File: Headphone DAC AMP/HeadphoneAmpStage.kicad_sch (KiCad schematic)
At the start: 66 parts, among them U3 TPA6120A2DWP, U4 OPA1612AxD, U5 OPA1612AxD

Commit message: Cleaned up shcematic more
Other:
- note added: "Amplifier Decoupling"
- note added: "Analog Filtering"
- note added: "Filter Decoupling"
- note added: "Headphone Amplifier"
- moved on the sheet: C25, C26, C27, C28, C29, C30, C31, C32, C5, C6, C7, C8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

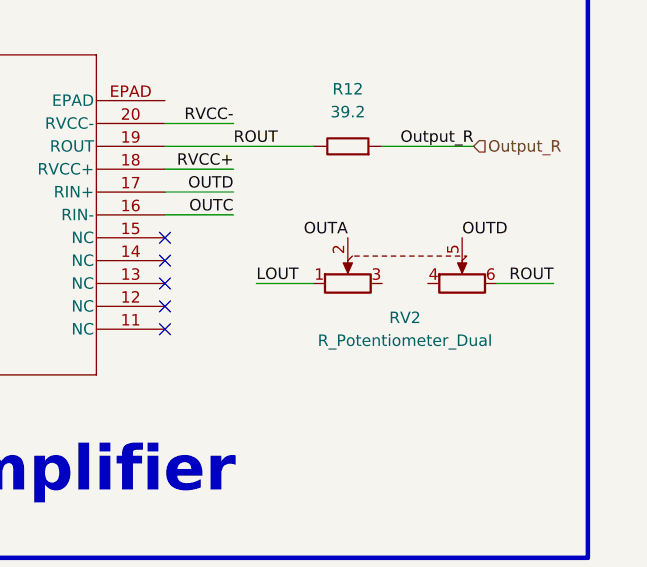
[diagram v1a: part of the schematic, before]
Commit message: Cleaned Up and Annotated Schematic
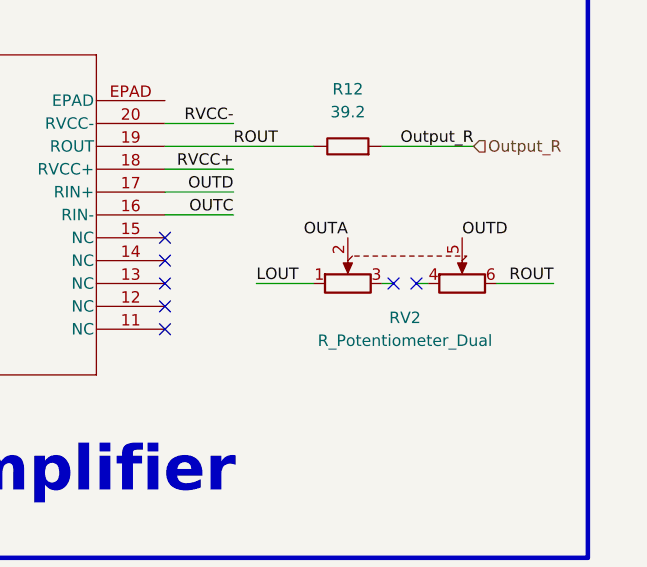
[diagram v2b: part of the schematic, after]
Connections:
- no-connect marks 10 -> 12
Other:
- company: (none) -> Personal Project - Kettering University
- title: (none) -> Hi-Fidelity USB DAC Amplifier
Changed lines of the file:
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@@
 	(generator_version "9.0")
 	(paper "A4")
+	(title_block
+		(title "Hi-Fidelity USB DAC Amplifier")
+		(date "2025-11-19")
+		(rev "1.0")
+		(company "Personal Project - Kettering University")
+		(comment 1 "Designed by Dan Abidov & Luke Stirzinger")
+		(comment 2 "Based on XMOS Xu316 and ES9039Q2M")
+	)
 	(rectangle
 		(start 12.7 12.7)
@@
 	)
 	(no_connect
+		(at 264.16 46.99)
+	)
+	(no_connect
 		(at 170.18 46.99)
 	)
@@
 	)
 	(no_connect
+		(at 261.62 46.99)
+	)
+	(no_connect
 		(at 236.22 41.91)
 	)
@@
 	(wire
 		(pts
+			(xy 264.16 46.99) (xy 265.43 46.99)
+		)
+		(stroke
+			(width 0)
+			(type default)
+		)
+	)
+	(wire
+		(pts
 			(xy 40.64 106.68) (xy 41.91 106.68)
 		)
@@
 	(wire
 		(pts
+			(xy 261.62 46.99) (xy 260.35 46.99)
+		)
+		(stroke
+			(width 0)
+			(type default)
+		)
+	)
+	(wire
+		(pts
 			(xy 243.84 36.83) (xy 236.22 36.83)
 		)
@@
 			"AAAAAAAAAAAAAAAAAAAAAAAAAAAAAAAAAAAAAAAAAAAAAAAAAAAAAAAAAAAAAAAAAAAAAAAAAAAA"
 			"AAAAAAAAAAAAAAAAAAAAAAAAAAAAAAAAAAAAAAAAAAAAAAAAAAAAAAAAAAAAAAAAAAAAAAAAAAAA"
+			"AAAAAAAAAAAAAAAAAAAAAAAAAAAAAAAAAAAAAAAAAAAAAAAAAAAAAAAAAAAAAAAAAAAAAAAAAAAA"
+			"AAAAAAAAAAAAAAAAAAAAAAAAAAAAAAAAAAAAAAAAAAAAAAAAAAAAAAAAAAAAAAAAAAAAAAAAAAAA"
+			"AAAAAAAAAAAAAAAAAAAAAAAAAAAAAAAAAAAAAAAAAAAAAAAAAAAAAAAAAAAAAAAAAAAAAAAAAAAA"
+			"AAAAAAAAAAAAAAAAAAAAAAAAAAAAAAAAAAAAAAAAAAAAAAAAAAAAAAAAAAAAAAAAAAAAAAAAAAAA"
+			"AAAAAAAAAAAAAAAAAAAAAAAAAAAAAAAAAAAAAAAAAAAAAAAAAAAAAAAAAAAAAAAAAAAAAAAAAAAA"
+			"AAAAAAAAAAAAAAAAAAAAAAAAAAAAAAAAAAAAAAAAAAAAAAAAAAAAAAAAAAAAAAAAAAAAAAAAAAAA"
+			"AAAAAAAAAAAAAAAAAAAAAAAAAAAAAAAAAAAAAAAAAAAAAAAAAAAAAAAAAAAAAAAAAAAAAAAAAAAA"
+			"AAAAAAAAAAAAAAAAAAAAAAAAAAAAAAAAAAAAAAAAAAAAAAAAAAAAAAAAAAAAAAAAAAAAAAAAAAAA"
+			"AAAAAAAAAAAAAAAAAAAAAAAAAAAAAAAAAAAAAAAAAAAAAAAAAAAAAAAAAAAAAAAAAAAAAAAAAAAA"
+			"AAAAAAAAAAAAAAAAAAAAAAAAAAAAAAAAAAAAAAAAAAAAAAAAAAAAAAAAAAAAAAAAAAAAAAAAAAAA"
+			"AAAAAAAAAAAAAAAAAAAAAAAAAAAAAAAAAAAAAAAAAAAAAAAAAAAAAAAAAAAAAAAAAAAAAAAAAAAA"
+			"AAAAAAAAAAAAAAAAAAAAAAAAAAAAAAAAAAAAAAAAAAAAAAAAAAAAAAAAAAAAAAAAAAAAAAAAAAAA"
+			"AAAAAAAAAAAAAAAAAAAAAAAAAAAAAAAAAAAAAAAAAAAAAAAAAAAAAAAAAAAAAAAAAAAAAAAAAAAA"
+			"AAAAAAAAAAAAAAAAAAAAAAAAAAAAAAAAAAAAAAAAAAAAAAAAAAAAAAAAAAAAAAAAAAAAAAAAAAAA"
+			"AAAAAAAAAAAAAAAAAAAAAAAAAAAAAAAAAAAAAAAAAAAAAAAAAAAAAAAAAAAAAAAAAAAAAAAAAAAA"
+			"AAAAAAAAAAAAAAAAAAAAAAAAAAAAAAAAAAAAAAAAAAAAAAAAAAAAAAAAAAAAAAAAAAAAAAAAAAAA"
+			"AAAAAAAAAAAAAAAAAAAAAAAAAAAAAAAAAAAAAAAAAAAAAAAAAAAAAAAAAAAAAAAAAAAAAAAAAAAA"
+			"AAAAAAAAAAAAAAAAAAAAAAAAAAAAAAAAAAAAAAAAAAAAAAAAAAAAAAAAAAAAAAAAAAAAAAAAAAAA"

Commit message: Schematic V1 Done
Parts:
- R11, R12: footprint Resistor_THT:R_Axial_DIN0207_L6.3mm_D2.5mm_P10.16mm_Horizontal -> Capacitor_SMD:C_0805_2012Metric_Pad1.18x1.45mm_HandSolder
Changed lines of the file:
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@@
 			"AAAAAAAAAAAAAAAAAAAAAAAAAAAAAAAAAAAAAAAAAAAAAAAAAAAAAAAAAAAAAAAAAAAAAAAAAAAA"
 			"AAAAAAAAAAAAAAAAAAAAAAAAAAAAAAAAAAAAAAAAAAAAAAAAAAAAAAAAAAAAAAAAAAAAAAAAAAAA"
+			"AAAAAAAAAAAAAAAAAAAAAAAAAAAAAAAAAAAAAAAAAAAAAAAAAAAAAAAAAAAAAAAAAAAAAAAAAAAA"
+			"AAAAAAAAAAAAAAAAAAAAAAAAAAAAAAAAAAAAAAAAAAAAAAAAAAAAAAAAAAAAAAAAAAAAAAAAAAAA"
+			"AAAAAAAAAAAAAAAAAAAAAAAAAAAAAAAAAAAAAAAAAAAAAAAAAAAAAAAAAAAAAAAAAAAAAAAAAAAA"
+			"AAAAAAAAAAAAAAAAAAAAAAAAAAAAAAAAAAAAAAAAAAAAAAAAAAAAAAAAAAAAAAAAAAAAAAAAAAAA"
+			"AAAAAAAAAAAAAAAAAAAAAAAAAAAAAAAAAAAAAAAAAAAAAAAAAAAAAAAAAAAAAAAAAAAAAAAAAAAA"
+			"AAAAAAAAAAAAAAAAAAAAAAAAAAAAAAAAAAAAAAAAAAAAAAAAAAAAAAAAAAAAAAAAAAAAAAAAAAAA"
+			"AAAAAAAAAAAAAAAAAAAAAAAAAAAAAAAAAAAAAAAAAAAAAAAAAAAAAAAAAAAAAAAAAAAAAAAAAAAA"
+			"AAAAAAAAAAAAAAAAAAAAAAAAAAAAAAAAAAAAAAAAAAAAAAAAAAAAAAAAAAAAAAAAAAAAAAAAAAAA"
+			"AAAAAAAAAAAAAAAAAAAAAAAAAAAAAAAAAAAAAAAAAAAAAAAAAAAAAAAAAAAAAAAAAAAAAAAAAAAA"
+			"AAAAAAAAAAAAAAAAAAAAAAAAAAAAAAAAAAAAAAAAAAAAAAAAAAAAAAAAAAAAAAAAAAAAAAAAAAAA"
+			"AAAAAAAAAAAAAAAAAAAAAAAAAAAAAAAAAAAAAAAAAAAAAAAAAAAAAAAAAAAAAAAAAAAAAAAAAAAA"
+			"AAAAAAAAAAAAAAAAAAAAAAAAAAAAAAAAAAAAAAAAAAAAAAAAAAAAAAAAAAAAAAAAAAAAAAAAAAAA"
+			"AAAAAAAAAAAAAAAAAAAAAAAAAAAAAAAAAAAAAAAAAAAAAAAAAAAAAAAAAAAAAAAAAAAAAAAAAAAA"
+			"AAAAAAAAAAAAAAAAAAAAAAAAAAAAAAAAAAAAAAAAAAAAAAAAAAAAAAAAAAAAAAAAAAAAAAAAAAAA"
+			"AAAAAAAAAAAAAAAAAAAAAAAAAAAAAAAAAAAAAAAAAAAAAAAAAAAAAAAAAAAAAAAAAAAAAAAAAAAA"
+			"AAAAAAAAAAAAAAAAAAAAAAAAAAAAAAAAAAAAAAAAAAAAAAAAAAAAAAAAAAAAAAAAAAAAAAAAAAAA"
+			"AAAAAAAAAAAAAAAAAAAAAAAAAAAAAAAAAAAAAAAAAAAAAAAAAAAAAAAAAAAAAAAAAAAAAAAAAAAA"
+			"AAAAAAAAAAAAAAAAAAAAAAAAAAAAAAAAAAAAAAAAAAAAAAAAAAAAAAAAAAAAAAAAAAAAAAAAAAAA"
 			"AAAAAAAAAAAAAAAAAAAAAAAAAAAAAAAAAAAAAAAAAAAAAAAAAA=="
 		)
@@
 		(exclude_from_sim no)
 		(in_bom yes)
-		(on_board yes)
+		(on_board no)
 		(dnp no)
 		(fields_autoplaced yes)
@@
 			)
 		)
-		(property "Footprint" "Resistor_THT:R_Axial_DIN0207_L6.3mm_D2.5mm_P10.16mm_Horizontal"
+		(property "Footprint" "Capacitor_SMD:C_0805_2012Metric_Pad1.18x1.45mm_HandSolder"
 			(at 156.591 24.892 0)
 			(effects
@@
 		(exclude_from_sim no)
 		(in_bom yes)
-		(on_board yes)
+		(on_board no)
 		(dnp no)
 		(fields_autoplaced yes)
@@
 			)
 		)
-		(property "Footprint" "Resistor_THT:R_Axial_DIN0207_L6.3mm_D2.5mm_P10.16mm_Horizontal"
+		(property "Footprint" "Capacitor_SMD:C_0805_2012Metric_Pad1.18x1.45mm_HandSolder"
 			(at 255.651 27.432 0)
 			(effects

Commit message: Fixed all the work i put in
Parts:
- removed C25, C28, C31: 400p, Capacitor_SMD:C_0805_2012Metric_Pad1.18x1.45mm_HandSolder, symbol Device:C
- removed C26, C29, C32: 110p, Capacitor_SMD:C_0805_2012Metric_Pad1.18x1.45mm_HandSolder, symbol Device:C
- removed C27, C30: 1p, Capacitor_SMD:C_0805_2012Metric_Pad1.18x1.45mm_HandSolder, symbol Device:C
- removed R10, R21, R6: 4.7k, Resistor_SMD:R_0805_2012Metric_Pad1.20x1.40mm_HandSolder, symbol Device:R
- removed R18, R22, R23, R9: 1k, Resistor_SMD:R_0805_2012Metric_Pad1.20x1.40mm_HandSolder, symbol Device:R
- removed R19, R7: 4.8k, Resistor_SMD:R_0805_2012Metric_Pad1.20x1.40mm_HandSolder, symbol Device:R
- removed R20, R5, R8: 4.7meg, Resistor_SMD:R_0805_2012Metric_Pad1.20x1.40mm_HandSolder, symbol Device:R
- removed unit 2 of U4
- removed unit 2 of U5
- C5: value 400p -> 2200p
- C6, C8: value 1p -> 2200p
- C7: value 110p -> 2200p
- R1, R4: value 4.8k -> 800
- R2: value 4.7meg -> 800
- R3: value 4.7k -> 800
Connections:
- net +Lin: now also C8.1, R4.1, U5.6 (-)
- net +Rin: now also C6.1, R2.1, U4.6 (-); no longer R4.1
- net -Lin: now also C7.1, R3.1, U5.2 (-)
- net -Rin: now also C5.1, U4.2 (-)
- net GND: now also U4.3 (+), U4.5 (+), U5.3 (+), U5.5 (+); no longer C6.2, C7.2, C8.2
- net OUTA: now also C5.2, R1.2, U4.1
- net OUTB: now also C6.2, R2.2, U4.7
- net OUTC: now also C7.2, R3.2, U5.1
- net OUTD: now also C8.2, R4.2, U5.7
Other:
- moved on the sheet: C5, R1

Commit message: Hopefully my mistakes are not for naught
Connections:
- net +Lin: no longer U5.6 (-)
- net GND: no longer U5.5 (+)
- net OUTD: no longer U5.7
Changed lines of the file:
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@@
 	)
 	(junction
-		(at 74.93 148.59)
-		(diameter 0)
-		(color 0 0 0 0)
-	)
-	(junction
 		(at 234.95 96.52)
 		(diameter 0)
@@
 	(symbol
 		(lib_id "Amplifier_Operational:OPA1612AxD")
-		(at 67.31 148.59 0)
+		(at 67.31 113.03 0)
 		(mirror x)
-		(unit 2)
+		(unit 1)
 		(exclude_from_sim no)
 		(in_bom yes)
 		(on_board yes)
 		(dnp no)
-		(fields_autoplaced yes)
 		(property "Reference" "U5"
-			(at 67.31 158.75 0)
+			(at 67.31 123.19 0)
 			(effects
 				(font
@@
 		)
 		(property "Value" "OPA1612AxD"
-			(at 67.31 140.97 0)
+			(at 70.612 118.11 0)
 			(effects
 				(font
@@
 		)
 		(property "Footprint" "Package_SO:SOIC-8-1EP_3.9x4.9mm_P1.27mm_EP2.95x4.9mm_Mask2.71x3.4mm_ThermalVias"
-			(at 67.31 148.59 0)
+			(at 67.31 113.03 0)
 			(effects
 				(font
@@
 		)
 		(property "Datasheet" "http://www.ti.com/lit/ds/symlink/opa1612.pdf"
-			(at 67.31 148.59 0)
+			(at 67.31 113.03 0)
 			(effects
 				(font
@@
 		)
 		(property "Description" "Dual SoundPlus High Performance, Bipolar-Input Audio Operational Amplifiers, SOIC-8"
-			(at 67.31 148.59 0)
+			(at 67.31 113.03 0)
 			(effects
 				(font
@@
 				(path "/d034eddd-efbc-47be-a25c-37cbfbab4cd8/a8d45096-939e-42db-8984-b3f2d55a20c4"
 					(reference "U5")
-					(unit 2)
+					(unit 1)
 				)
 			)
@@
 	(symbol
 		(lib_id "Amplifier_Operational:OPA1612AxD")
-		(at 67.31 113.03 0)
+		(at 90.17 142.24 0)
 		(mirror x)
-		(unit 1)
+		(unit 2)
 		(exclude_from_sim no)
 		(in_bom yes)
 		(on_board yes)
 		(dnp no)
+		(fields_autoplaced yes)
 		(property "Reference" "U5"
-			(at 67.31 123.19 0)
+			(at 90.17 152.4 0)
 			(effects
 				(font
@@
 		)
 		(property "Value" "OPA1612AxD"
-			(at 70.612 118.11 0)
+			(at 90.17 134.62 0)
 			(effects
 				(font
@@
 		)
 		(property "Footprint" "Package_SO:SOIC-8-1EP_3.9x4.9mm_P1.27mm_EP2.95x4.9mm_Mask2.71x3.4mm_ThermalVias"
-			(at 67.31 113.03 0)
+			(at 90.17 142.24 0)
 			(effects
 				(font
@@
 		)
 		(property "Datasheet" "http://www.ti.com/lit/ds/symlink/opa1612.pdf"
-			(at 67.31 113.03 0)
+			(at 90.17 142.24 0)
 			(effects
 				(font
@@
 		)
 		(property "Description" "Dual SoundPlus High Performance, Bipolar-Input Audio Operational Amplifiers, SOIC-8"
-			(at 67.31 113.03 0)
+			(at 90.17 142.24 0)
 			(effects
 				(font
@@
 				(path "/d034eddd-efbc-47be-a25c-37cbfbab4cd8/a8d45096-939e-42db-8984-b3f2d55a20c4"
 					(reference "U5")
-					(unit 1)
+					(unit 2)
 				)
 			)
@@
 	(symbol
 		(lib_id "Amplifier_Operational:OPA1612AxD")
-		(at 66.04 40.64 0)
+		(at 66.04 77.47 0)
 		(mirror x)
-		(unit 1)
+		(unit 2)
 		(exclude_from_sim no)
 		(in_bom yes)
 		(on_board yes)
 		(dnp no)
+		(fields_autoplaced yes)
 		(property "Reference" "U4"
-			(at 66.04 50.8 0)
+			(at 66.04 87.63 0)
 			(effects
 				(font
@@
 		)
 		(property "Value" "OPA1612AxD"
-			(at 69.342 45.72 0)
+			(at 66.04 69.85 0)
 			(effects
 				(font
@@
 		)
 		(property "Footprint" "Package_SO:SOIC-8-1EP_3.9x4.9mm_P1.27mm_EP2.95x4.9mm_Mask2.71x3.4mm_ThermalVias"
-			(at 66.04 40.64 0)
+			(at 66.04 77.47 0)
 			(effects
 				(font
@@
 		)
 		(property "Datasheet" "http://www.ti.com/lit/ds/symlink/opa1612.pdf"
-			(at 66.04 40.64 0)
+			(at 66.04 77.47 0)
 			(effects
 				(font
@@
 		)
 		(property "Description" "Dual SoundPlus High Performance, Bipolar-Input Audio Operational Amplifiers, SOIC-8"
-			(at 66.04 40.64 0)
+			(at 66.04 77.47 0)
 			(effects
 				(font
@@
 				(path "/d034eddd-efbc-47be-a25c-37cbfbab4cd8/a8d45096-939e-42db-8984-b3f2d55a20c4"
 					(reference "U4")
-					(unit 1)
+					(unit 2)
 				)
 			)
@@
 	(symbol
 		(lib_id "Amplifier_Operational:OPA1612AxD")
-		(at 66.04 77.47 0)
+		(at 66.04 40.64 0)
 		(mirror x)
-		(unit 2)
+		(unit 1)
 		(exclude_from_sim no)
 		(in_bom yes)
 		(on_board yes)
 		(dnp no)
-		(fields_autoplaced yes)
 		(property "Reference" "U4"
-			(at 66.04 87.63 0)
+			(at 66.04 50.8 0)
 			(effects
 				(font
@@
 		)
 		(property "Value" "OPA1612AxD"
-			(at 66.04 69.85 0)
+			(at 69.342 45.72 0)
 			(effects
 				(font
@@
 		)
 		(property "Footprint" "Package_SO:SOIC-8-1EP_3.9x4.9mm_P1.27mm_EP2.95x4.9mm_Mask2.71x3.4mm_ThermalVias"
-			(at 66.04 77.47 0)
+			(at 66.04 40.64 0)
 			(effects
 				(font
@@
 		)
 		(property "Datasheet" "http://www.ti.com/lit/ds/symlink/opa1612.pdf"
-			(at 66.04 77.47 0)
+			(at 66.04 40.64 0)
 			(effects
 				(font
@@
 		)
 		(property "Description" "Dual SoundPlus High Performance, Bipolar-Input Audio Operational Amplifiers, SOIC-8"
-			(at 66.04 77.47 0)
+			(at 66.04 40.64 0)
 			(effects
 				(font
@@
 				(path "/d034eddd-efbc-47be-a25c-37cbfbab4cd8/a8d45096-939e-42db-8984-b3f2d55a20c4"
 					(reference "U4")
-					(unit 2)
+					(unit 1)
 				)
 			)

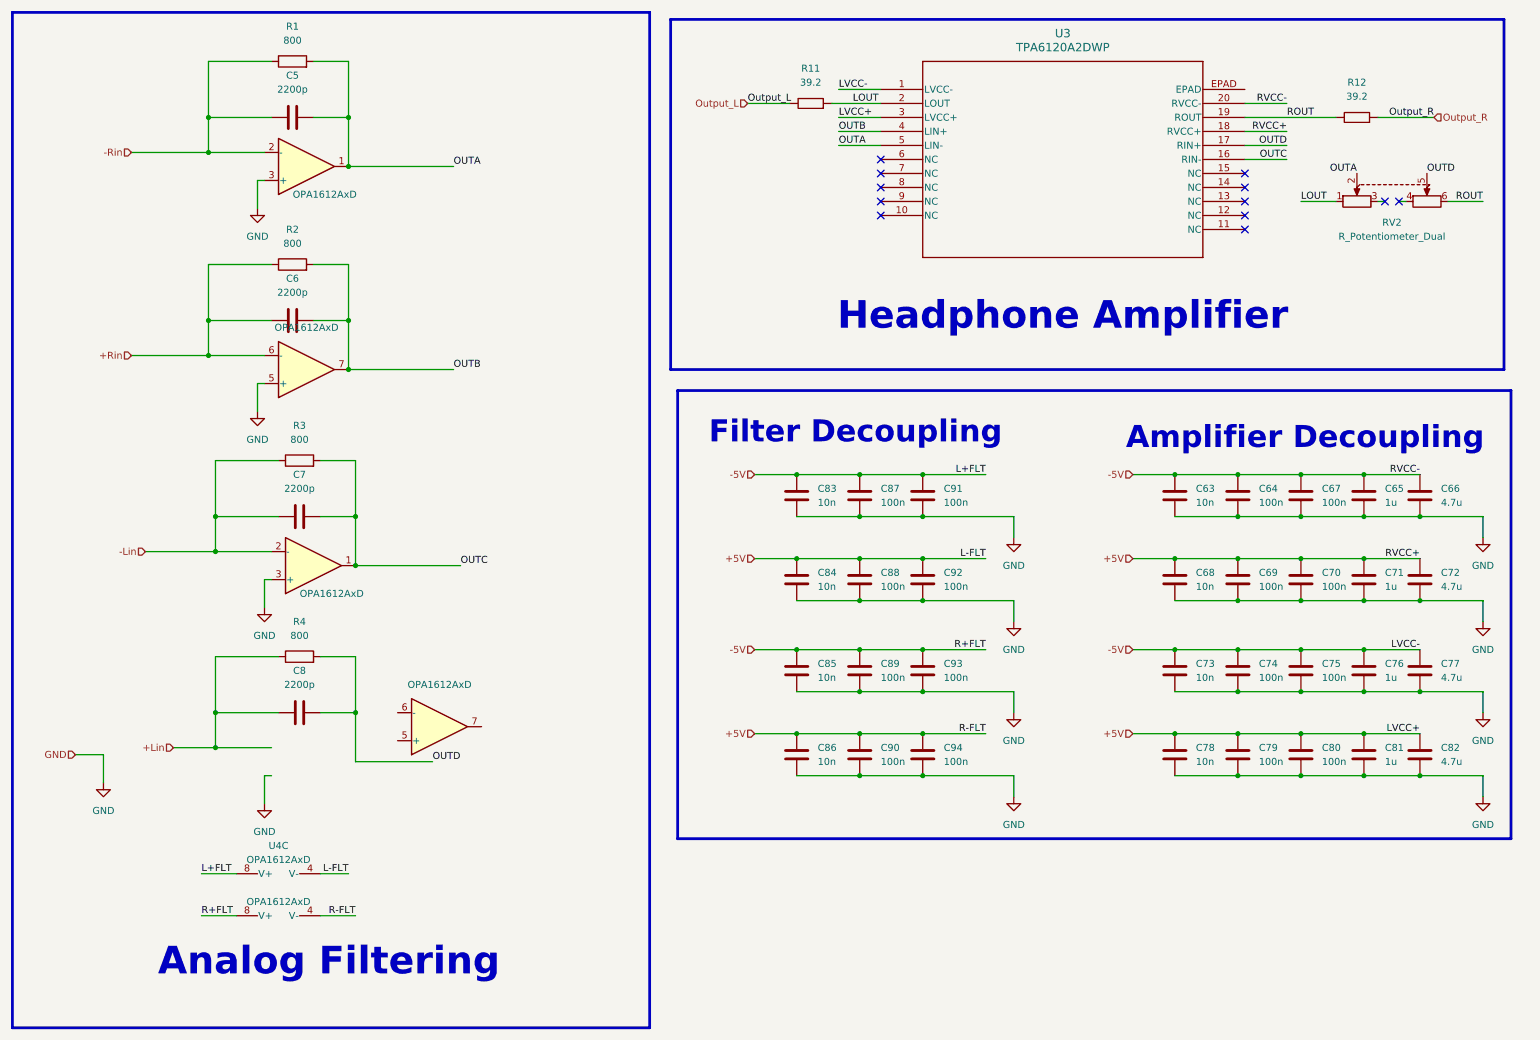
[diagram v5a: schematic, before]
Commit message: Footprints & Placements
All footprints are loaded in PCB error free, some PCB mistakes were fixed, and worked on the placements for the TPA6120, the XMOS, the DAC, and the outputs
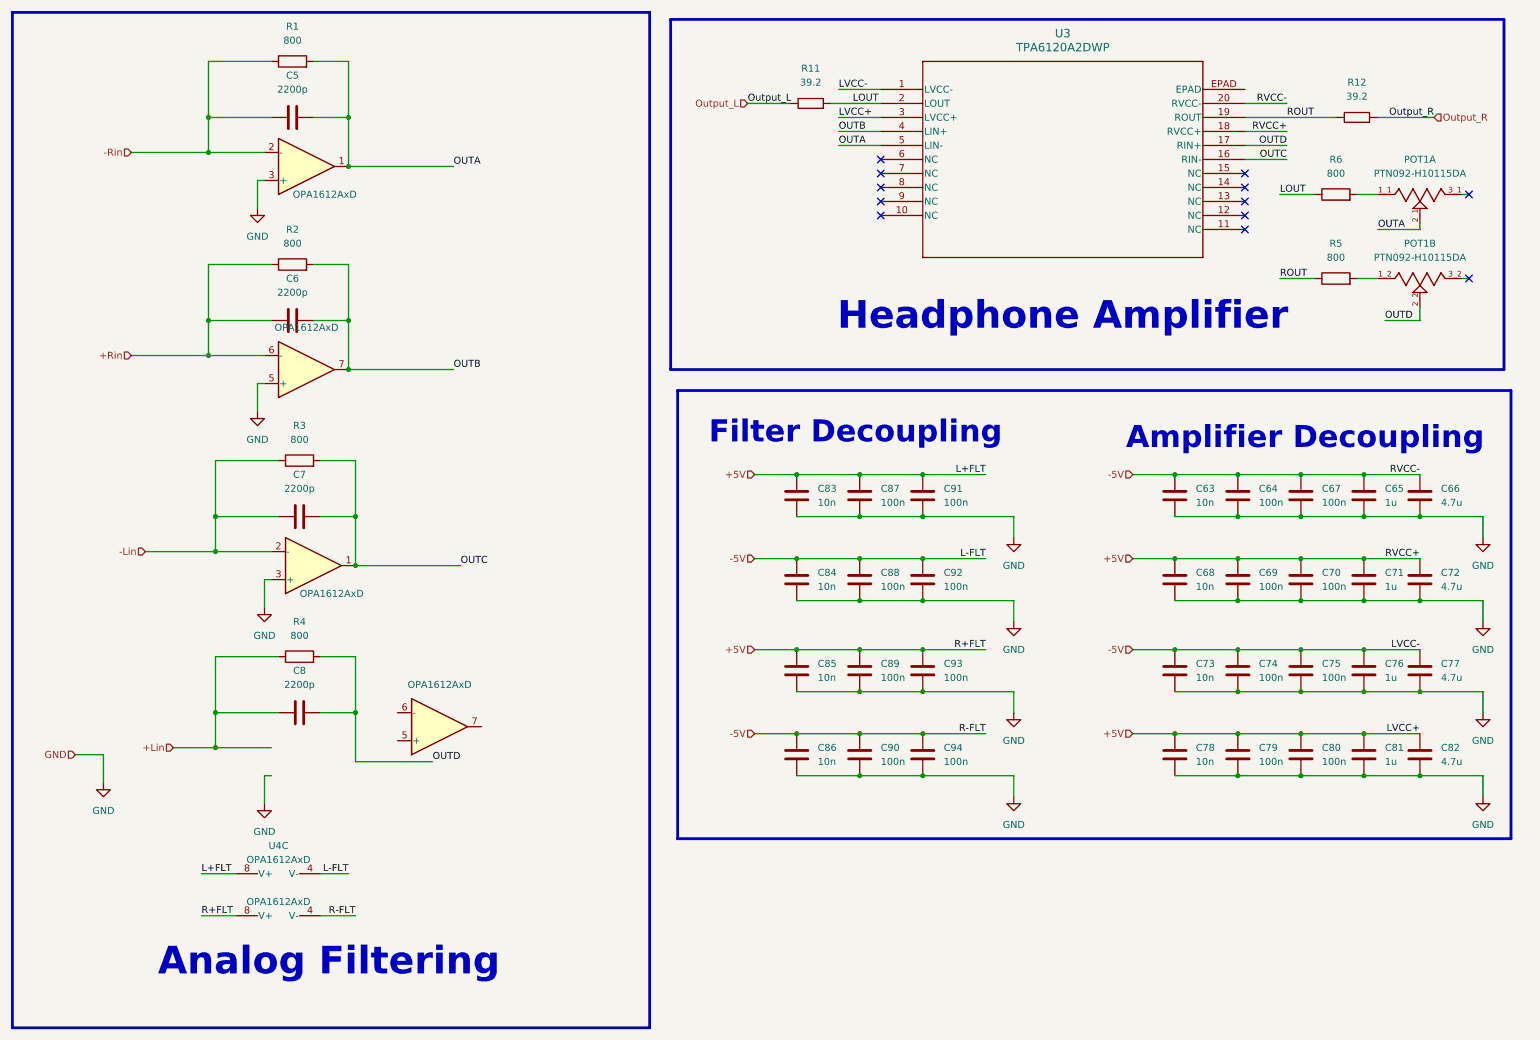
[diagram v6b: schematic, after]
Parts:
- removed RV2: R_Potentiometer_Dual, symbol Device:R_Potentiometer_Dual
- added POT1: PTN092-H10115DA, PTN092-H10115DA:TRIM_PTN092-H10115DA, symbol PTN092-H10115DA:PTN092-H10115DA
- added R5, R6: 800, Resistor_SMD:R_0805_2012Metric_Pad1.20x1.40mm_HandSolder, symbol Device:R
- added unit 1 of U4
- added unit 2 of U5
- R11, R12: footprint Capacitor_SMD:C_0805_2012Metric_Pad1.18x1.45mm_HandSolder -> Resistor_SMD:R_0805_2012Metric_Pad1.20x1.40mm_HandSolder
- U3: footprint DWP20_3P81X2P79 -> footprints:TPA6120A2DWP
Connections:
- net +5V: now also C83.1, C85.1, C87.1, C89.1, C91.1, C93.1, U4.8 (V+), U5.8 (V+); no longer C84.1, C86.1, C88.1, C90.1, C92.1, C94.1, U4.4 (V-), U5.4 (V-)
- net -5V: now also C84.1, C86.1, C88.1, C90.1, C92.1, C94.1, U4.4 (V-), U5.4 (V-); no longer C83.1, C85.1, C87.1, C89.1, C91.1, C93.1, U4.8 (V+), U5.8 (V+)
- net -Rin: now also U4.2 (-); no longer U4.2 (-)
- net GND: now also U4.3 (+); no longer U4.3 (+)
- net LOUT: now also R6.1
- net OUTA: now also POT1.2_1, U4.1; no longer U4.1
- net OUTD: now also POT1.2_2
- net ROUT: now also R5.1
- new net: POT1.1_1, R6.2
- new net: POT1.1_2, R5.2

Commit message: Printed
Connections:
- net +Lin: now also U5.6 (-)
- net GND: now also U5.5 (+)
- net OUTD: now also U5.7
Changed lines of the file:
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@@
 	)
 	(junction
+		(at 74.93 148.59)
+		(diameter 0)
+		(color 0 0 0 0)
+	)
+	(junction
 		(at 257.81 119.38)
 		(diameter 0)
@@
 	(wire
 		(pts
-			(xy 74.93 148.59) (xy 88.9 148.59)
+			(xy 74.93 148.59) (xy 87.63 148.59)
 		)
 		(stroke
@@
 	)
 	(label "OUTD"
-		(at 88.9 148.59 0)
+		(at 87.63 148.59 0)
 		(effects
 			(font
@@
 	(symbol
 		(lib_id "Amplifier_Operational:OPA1612AxD")
-		(at 90.17 142.24 0)
+		(at 67.31 148.59 0)
 		(mirror x)
 		(unit 2)
@@
 		(fields_autoplaced yes)
 		(property "Reference" "U5"
-			(at 90.17 152.4 0)
+			(at 67.31 158.75 0)
 			(effects
 				(font
@@
 		)
 		(property "Value" "OPA1612AxD"
-			(at 90.17 134.62 0)
+			(at 67.31 140.97 0)
 			(effects
 				(font
@@
 		)
 		(property "Footprint" "Package_SO:SOIC-8-1EP_3.9x4.9mm_P1.27mm_EP2.95x4.9mm_Mask2.71x3.4mm_ThermalVias"
-			(at 90.17 142.24 0)
+			(at 67.31 148.59 0)
 			(effects
 				(font
@@
 		)
 		(property "Datasheet" "http://www.ti.com/lit/ds/symlink/opa1612.pdf"
-			(at 90.17 142.24 0)
+			(at 67.31 148.59 0)
 			(effects
 				(font
@@
 		)
 		(property "Description" "Dual SoundPlus High Performance, Bipolar-Input Audio Operational Amplifiers, SOIC-8"
-			(at 90.17 142.24 0)
+			(at 67.31 148.59 0)
 			(effects
 				(font
